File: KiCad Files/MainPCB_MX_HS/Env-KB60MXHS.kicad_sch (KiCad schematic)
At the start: 157 parts, among them J1 Conn_01x04, SW1 EVQ-P7A01P, U1 Pico

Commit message: modified mount holes for future test
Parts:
- H1, H10, H11, H2, H3, H4, H5, H6, H7, H9: footprint Env_Extras:MountingHole_2.2mm_M2-MODIFIED -> MountingHole:MountingHole_3.5mm_Pad
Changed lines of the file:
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@@
       (effects (font (size 1.27 1.27)) (justify left))
     )
-    (property "Footprint" "Env_Extras:MountingHole_2.2mm_M2-MODIFIED" (id 2) (at 162.56 176.53 0)
+    (property "Footprint" "MountingHole:MountingHole_3.5mm_Pad" (id 2) (at 162.56 176.53 0)
       (effects (font (size 1.27 1.27)) hide)
     )
@@
       (effects (font (size 1.27 1.27)) (justify left))
     )
-    (property "Footprint" "Env_Extras:MountingHole_2.2mm_M2-MODIFIED" (id 2) (at 162.56 181.61 0)
+    (property "Footprint" "MountingHole:MountingHole_3.5mm_Pad" (id 2) (at 162.56 181.61 0)
       (effects (font (size 1.27 1.27)) hide)
     )
@@
       (effects (font (size 1.27 1.27)) (justify left))
     )
-    (property "Footprint" "Env_Extras:MountingHole_2.2mm_M2-MODIFIED" (id 2) (at 162.56 186.69 0)
+    (property "Footprint" "MountingHole:MountingHole_3.5mm_Pad" (id 2) (at 162.56 186.69 0)
       (effects (font (size 1.27 1.27)) hide)
     )
@@
       (effects (font (size 1.27 1.27)) (justify left))
     )
-    (property "Footprint" "Env_Extras:MountingHole_2.2mm_M2-MODIFIED" (id 2) (at 162.56 191.77 0)
+    (property "Footprint" "MountingHole:MountingHole_3.5mm_Pad" (id 2) (at 162.56 191.77 0)
       (effects (font (size 1.27 1.27)) hide)
     )
@@
       (effects (font (size 1.27 1.27)) (justify left))
     )
-    (property "Footprint" "Env_Extras:MountingHole_2.2mm_M2-MODIFIED" (id 2) (at 162.56 201.93 0)
+    (property "Footprint" "MountingHole:MountingHole_3.5mm_Pad" (id 2) (at 162.56 201.93 0)
       (effects (font (size 1.27 1.27)) hide)
     )
@@
       (effects (font (size 1.27 1.27)) (justify left))
     )
-    (property "Footprint" "Env_Extras:MountingHole_2.2mm_M2-MODIFIED" (id 2) (at 162.56 207.01 0)
+    (property "Footprint" "MountingHole:MountingHole_3.5mm_Pad" (id 2) (at 162.56 207.01 0)
       (effects (font (size 1.27 1.27)) hide)
     )
@@
       (effects (font (size 1.27 1.27)) (justify left))
     )
-    (property "Footprint" "Env_Extras:MountingHole_2.2mm_M2-MODIFIED" (id 2) (at 162.56 161.29 0)
+    (property "Footprint" "MountingHole:MountingHole_3.5mm_Pad" (id 2) (at 162.56 161.29 0)
       (effects (font (size 1.27 1.27)) hide)
     )
@@
       (effects (font (size 1.27 1.27)) (justify left))
     )
-    (property "Footprint" "Env_Extras:MountingHole_2.2mm_M2-MODIFIED" (id 2) (at 162.56 166.37 0)
+    (property "Footprint" "MountingHole:MountingHole_3.5mm_Pad" (id 2) (at 162.56 166.37 0)
       (effects (font (size 1.27 1.27)) hide)
     )
@@
       (effects (font (size 1.27 1.27)) (justify left))
     )
-    (property "Footprint" "Env_Extras:MountingHole_2.2mm_M2-MODIFIED" (id 2) (at 162.56 171.45 0)
+    (property "Footprint" "MountingHole:MountingHole_3.5mm_Pad" (id 2) (at 162.56 171.45 0)
       (effects (font (size 1.27 1.27)) hide)
     )
@@
       (effects (font (size 1.27 1.27)) (justify left))
     )
-    (property "Footprint" "Env_Extras:MountingHole_2.2mm_M2-MODIFIED" (id 2) (at 162.56 196.85 0)
+    (property "Footprint" "MountingHole:MountingHole_3.5mm_Pad" (id 2) (at 162.56 196.85 0)
       (effects (font (size 1.27 1.27)) hide)
     )
@@
     )
     (path "/00000000-0000-0000-0000-0000608ab119"
-      (reference "H1") (unit 1) (value "SMTSO2020CTJ") (footprint "Env_Extras:MountingHole_2.2mm_M2-MODIFIED")
+      (reference "H1") (unit 1) (value "SMTSO2020CTJ") (footprint "MountingHole:MountingHole_3.5mm_Pad")
     )
     (path "/00000000-0000-0000-0000-0000609389ef"
-      (reference "H2") (unit 1) (value "SMTSO2020CTJ") (footprint "Env_Extras:MountingHole_2.2mm_M2-MODIFIED")
+      (reference "H2") (unit 1) (value "SMTSO2020CTJ") (footprint "MountingHole:MountingHole_3.5mm_Pad")
     )
     (path "/00000000-0000-0000-0000-0000608acb73"
-      (reference "H3") (unit 1) (value "SMTSO2020CTJ") (footprint "Env_Extras:MountingHole_2.2mm_M2-MODIFIED")
+      (reference "H3") (unit 1) (value "SMTSO2020CTJ") (footprint "MountingHole:MountingHole_3.5mm_Pad")
     )
     (path "/00000000-0000-0000-0000-0000609389f5"
-      (reference "H4") (unit 1) (value "SMTSO2020CTJ") (footprint "Env_Extras:MountingHole_2.2mm_M2-MODIFIED")
+      (reference "H4") (unit 1) (value "SMTSO2020CTJ") (footprint "MountingHole:MountingHole_3.5mm_Pad")
     )
     (path "/00000000-0000-0000-0000-0000608bcf9c"
-      (reference "H5") (unit 1) (value "SMTSO2020CTJ") (footprint "Env_Extras:MountingHole_2.2mm_M2-MODIFIED")
+      (reference "H5") (unit 1) (value "SMTSO2020CTJ") (footprint "MountingHole:MountingHole_3.5mm_Pad")
     )
     (path "/00000000-0000-0000-0000-0000609389fb"
-      (reference "H6") (unit 1) (value "SMTSO2020CTJ") (footprint "Env_Extras:MountingHole_2.2mm_M2-MODIFIED")
+      (reference "H6") (unit 1) (value "SMTSO2020CTJ") (footprint "MountingHole:MountingHole_3.5mm_Pad")
     )
     (path "/00000000-0000-0000-0000-0000608cd285"
-      (reference "H7") (unit 1) (value "SMTSO2020CTJ") (footprint "Env_Extras:MountingHole_2.2mm_M2-MODIFIED")
+      (reference "H7") (unit 1) (value "SMTSO2020CTJ") (footprint "MountingHole:MountingHole_3.5mm_Pad")
     )
     (path "/00000000-0000-0000-0000-0000608dd691"
-      (reference "H9") (unit 1) (value "SMTSO2020CTJ") (footprint "Env_Extras:MountingHole_2.2mm_M2-MODIFIED")
+      (reference "H9") (unit 1) (value "SMTSO2020CTJ") (footprint "MountingHole:MountingHole_3.5mm_Pad")
     )
     (path "/00000000-0000-0000-0000-0000608edb63"
-      (reference "H10") (unit 1) (value "SMTSO2020CTJ") (footprint "Env_Extras:MountingHole_2.2mm_M2-MODIFIED")
+      (reference "H10") (unit 1) (value "SMTSO2020CTJ") (footprint "MountingHole:MountingHole_3.5mm_Pad")
     )
     (path "/00000000-0000-0000-0000-0000609431fd"
-      (reference "H11") (unit 1) (value "SMTSO2020CTJ") (footprint "Env_Extras:MountingHole_2.2mm_M2-MODIFIED")
+      (reference "H11") (unit 1) (value "SMTSO2020CTJ") (footprint "MountingHole:MountingHole_3.5mm_Pad")
     )
     (path "/ad188452-862f-4110-adcf-92ca74aeb0da"

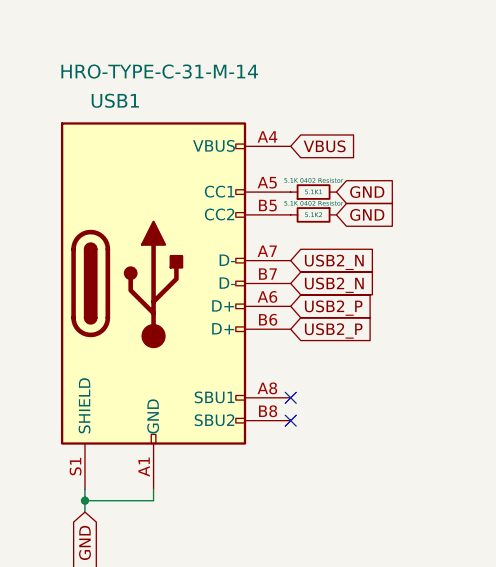
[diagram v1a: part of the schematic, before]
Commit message: updated hotswap version to have SMT compatible diode footprints
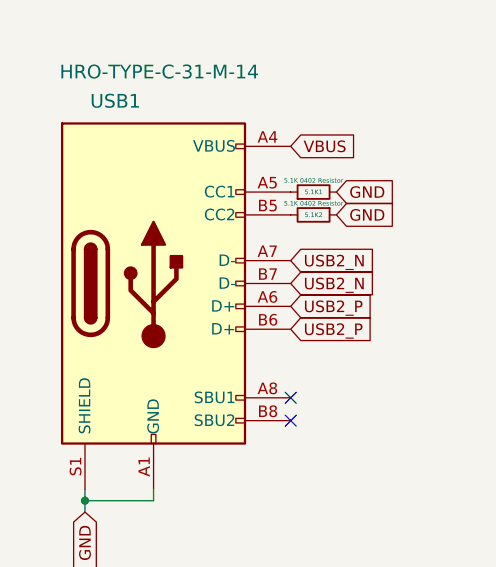
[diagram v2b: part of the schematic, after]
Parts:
- D_1, D_10, D_11, D_12, D_13, D_14, D_15, D_16, D_17, D_18, D_19, D_2, D_20, D_21, D_22, D_23, D_24, D_25, D_26, D_27, D_28, D_29, D_3, D_30, D_31, D_32, D_33, D_34, D_35, D_36, D_37, D_38, D_39, D_4, D_40, D_41, D_42, D_43, D_44, D_45, D_46, D_47, D_48, D_49, D_5, D_50, D_51, D_52, D_53, D_54, D_55, D_56, D_57, D_58, D_59, D_590, D_591, D_6, D_60, D_61, D_62, D_63, D_7, D_8, D_9: footprint Diode_THT:D_DO-35_SOD27_P7.62mm_Horizontal -> Env_Extras:SOD-123+D_DO-35_SOD27_P7.62mm_Horizontal

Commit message: generated gerbers
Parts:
- D_1, D_10, D_11, D_12, D_13, D_14, D_15, D_16, D_17, D_18, D_19, D_2, D_20, D_21, D_22, D_23, D_24, D_25, D_26, D_27, D_28, D_29, D_3, D_30, D_31, D_32, D_33, D_34, D_35, D_36, D_37, D_38, D_39, D_4, D_40, D_41, D_42, D_43, D_44, D_45, D_46, D_47, D_48, D_49, D_5, D_50, D_51, D_52, D_53, D_54, D_55, D_56, D_57, D_58, D_59, D_590, D_591, D_6, D_60, D_61, D_62, D_63, D_7, D_8, D_9: value D -> 1n4148W

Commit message: fixed issues with alignment
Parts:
- added stab9: MX Stabilizer, Mounting_Keyboard_Stabilizer:Stabilizer_Cherry_MX_6.25u, symbol Mechanical:MountingHole
- H1, H10, H11, H2, H3, H4, H5, H6, H7, H9: value SMTSO2020CTJ -> SMTSO2035CTJ

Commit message: fixed alignment issues, generated gerbers, fixed silkscreen issues, fixed footprints, generated gerbers
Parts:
- H1, H10, H11, H2, H3, H4, H5, H6, H7, H9: footprint MountingHole:MountingHole_3.5mm_Pad -> Env_Extras:MountingHole_2.2mm_M2-MODIFIED
- K_1, K_10, K_11, K_12, K_13, K_14, K_15, K_16, K_17, K_18, K_19, K_2, K_20, K_21, K_22, K_23, K_24, K_25, K_26, K_27, K_28, K_29, K_3, K_30, K_31, K_32, K_33, K_34, K_35, K_36, K_37, K_38, K_39, K_4, K_40, K_41, K_42, K_43, K_44, K_45, K_46, K_47, K_48, K_49, K_5, K_50, K_51, K_52, K_53, K_54, K_55, K_56, K_57, K_58, K_59, K_6, K_60, K_61, K_610, K_612, K_62, K_63, K_64, K_65, K_7, K_8, K_9: footprint MX_Only:MXOnly-1U-Hotswap-Modified -> Env_Extras:MXOnly-1U-Hotswap-Modified

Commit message: updated BOM,CPL to include missing parts needed, updated the values
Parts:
- D_1, D_10, D_11, D_12, D_13, D_14, D_15, D_16, D_17, D_18, D_19, D_2, D_20, D_21, D_22, D_23, D_24, D_25, D_26, D_27, D_28, D_29, D_3, D_30, D_31, D_32, D_33, D_34, D_35, D_36, D_37, D_38, D_39, D_4, D_40, D_41, D_42, D_43, D_44, D_45, D_46, D_47, D_48, D_49, D_5, D_50, D_51, D_52, D_53, D_54, D_55, D_56, D_57, D_58, D_59, D_590, D_591, D_6, D_60, D_61, D_62, D_63, D_7, D_8, D_9: value 1n4148W -> LL4148
- D_64: value 1n4007 SOD-123 -> 1n5817W
- K_1, K_10, K_11, K_12, K_13, K_14, K_15, K_16, K_17, K_18, K_19, K_2, K_20, K_21, K_22, K_23, K_24, K_25, K_26, K_27, K_28, K_29, K_3, K_30, K_31, K_32, K_33, K_34, K_35, K_36, K_37, K_38, K_39, K_4, K_40, K_41, K_42, K_43, K_44, K_45, K_46, K_47, K_48, K_49, K_5, K_50, K_51, K_52, K_53, K_54, K_55, K_56, K_57, K_58, K_59, K_6, K_60, K_61, K_610, K_612, K_62, K_63, K_64, K_65, K_7, K_8, K_9: value KEYSW -> CPG151101S11
- SW1: value EVQ-P7A01P -> EVQPUL; footprint PanasonicEVQ-P7A01P:Panasonic-EVQ-P7A01P-0-0-MFG -> Button_Switch_SMD:Panasonic_EVQPUL_EVQPUC
- USB1: value HRO-TYPE-C-31-M-14 -> TYPE-C-31-M-14
- stab1, stab2, stab3, stab4, stab5, stab6, stab7, stab8, stab9: now left out of the parts list

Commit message: Corrected Several issues pointed out by Dasky (tyvm), reduced top cover size to not conflict with the plate, swapped oled header power for correct voltage, extended several pads to make it easier to hand solder, extended stabiliser slots to make board outline less sharp,
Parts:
- 5.1K1, 5.1K2: value 5.1K 0402 Resistor -> 5.1K 0805 Resistor; footprint Resistor_THT:R_Axial_DIN0207_L6.3mm_D2.5mm_P10.16mm_Horizontal -> Resistor_SMD:R_0805_2012Metric_Pad1.20x1.40mm_HandSolder
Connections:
- net VSYS: no longer J1.3 (Pin_3)
- net at U1.36 (3V3): now also J1.3 (Pin_3)
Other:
- moved on the sheet: J1
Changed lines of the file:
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@@
 	)
 	(junction
-		(at 107.95 185.42)
-		(diameter 0)
-		(color 0 0 0 0)
-	)
-	(junction
 		(at 59.69 35.56)
 		(diameter 0)
@@
 	(wire
 		(pts
-			(xy 107.95 162.56) (xy 107.95 185.42)
-		)
-		(stroke
-			(width 0)
-			(type default)
-		)
-	)
-	(wire
-		(pts
 			(xy 325.12 74.93) (xy 325.12 49.53)
 		)
@@
 	(wire
 		(pts
-			(xy 107.95 185.42) (xy 106.68 185.42)
-		)
-		(stroke
-			(width 0)
-			(type default)
-		)
-	)
-	(wire
-		(pts
 			(xy 242.57 24.13) (xy 248.92 24.13)
 		)
@@
 	(wire
 		(pts
-			(xy 125.73 162.56) (xy 107.95 162.56)
+			(xy 124.46 193.04) (xy 106.68 193.04)
 		)
 		(stroke
@@
 	(wire
 		(pts
-			(xy 110.49 185.42) (xy 107.95 185.42)
+			(xy 106.68 185.42) (xy 110.49 185.42)
 		)
 		(stroke
@@
 	(global_label "GND"
 		(shape input)
-		(at 125.73 165.1 180)
+		(at 124.46 195.58 180)
 		(fields_autoplaced yes)
 		(effects
@@
 		)
 		(property "Intersheetrefs" "${INTERSHEET_REFS}"
-			(at 232.41 353.06 0)
+			(at 231.14 383.54 0)
 			(effects
 				(font
@@
 	(global_label "VSYS"
 		(shape input)
-		(at 107.95 171.45 0)
+		(at 109.855 185.42 90)
 		(fields_autoplaced yes)
 		(effects
@@
 		)
 		(property "Intersheetrefs" "${INTERSHEET_REFS}"
-			(at 114.8704 171.3706 0)
+			(at 109.855 178.4928 90)
 			(effects
 				(font
@@
 	(global_label "SDA"
 		(shape input)
-		(at 125.73 157.48 180)
+		(at 124.46 187.96 180)
 		(fields_autoplaced yes)
 		(effects
@@
 		)
 		(property "Intersheetrefs" "${INTERSHEET_REFS}"
-			(at 119.8377 157.4006 0)
+			(at 118.5677 187.8806 0)
 			(effects
 				(font
@@
 	(global_label "SCL"
 		(shape input)
-		(at 125.73 160.02 180)
+		(at 124.46 190.5 180)
 		(fields_autoplaced yes)
 		(effects
@@
 		)
 		(property "Intersheetrefs" "${INTERSHEET_REFS}"
-			(at 119.8982 159.9406 0)
+			(at 118.6282 190.4206 0)
 			(effects
 				(font
@@
 			)
 		)
-		(property "Value" "5.1K 0402 Resistor"
+		(property "Value" "5.1K 0805 Resistor"
 			(at 41.91 165.1 90)
 			(effects
@@
 			)
 		)
-		(property "Footprint" "Resistor_THT:R_Axial_DIN0207_L6.3mm_D2.5mm_P10.16mm_Horizontal"
+		(property "Footprint" "Resistor_SMD:R_0805_2012Metric_Pad1.20x1.40mm_HandSolder"
 			(at 41.91 166.37 0)
 			(effects
@@
 			)
 		)
-		(property "Value" "5.1K 0402 Resistor"
+		(property "Value" "5.1K 0805 Resistor"
 			(at 41.91 162.56 90)
 			(effects
@@
 			)
 		)
-		(property "Footprint" "Resistor_THT:R_Axial_DIN0207_L6.3mm_D2.5mm_P10.16mm_Horizontal"
+		(property "Footprint" "Resistor_SMD:R_0805_2012Metric_Pad1.20x1.40mm_HandSolder"
 			(at 41.91 163.83 0)
 			(effects
@@
 	(symbol
 		(lib_id "Connector_Generic:Conn_01x04")
-		(at 130.81 160.02 0)
+		(at 129.54 190.5 0)
 		(unit 1)
 		(exclude_from_sim no)
@@
 		(fields_autoplaced yes)
 		(property "Reference" "J1"
-			(at 133.35 160.0199 0)
+			(at 132.08 190.4999 0)
 			(effects
 				(font
@@
 		)
 		(property "Value" "Conn_01x04"
-			(at 133.35 162.5599 0)
+			(at 132.08 193.0399 0)
 			(effects
 				(font
@@
 		)
 		(property "Footprint" "Connector_PinSocket_2.54mm:PinSocket_1x04_P2.54mm_Vertical"
-			(at 130.81 160.02 0)
+			(at 129.54 190.5 0)
 			(effects
 				(font
@@
 		)
 		(property "Datasheet" "~"
-			(at 130.81 160.02 0)
+			(at 129.54 190.5 0)
 			(effects
 				(font
@@
 		)
 		(property "Description" ""
-			(at 130.81 160.02 0)
+			(at 129.54 190.5 0)
 			(effects
 				(font
